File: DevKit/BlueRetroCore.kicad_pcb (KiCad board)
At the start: 4 copper layers, 85 x 56 mm, 106 parts, among them J1 USB_C_Receptacle_USB2.0, J2 Conn_02x06, J3 Micro_SD_Card, J4 Conn_01x03, J5 DB25_Female, J6 Conn_02x13, J7 Conn_02x07, Q1 BSS138, Q2 BSS138, Q3 S8050, Q4 S8050, Q5 S8050, SW1 BOOT, SW2 EN, U1 ESP32-WROOM-32E, U10 TPD6F003, U11 TPD6F003, U12 TPD6F003, U13 TPD6F003, U2 FT2232HL, U3 STL6N3LLH6, U4 TCPP01-M12, U5 M93C46, U6 ECMF02-2AMX6, U7 TPD6F003, U8 AP7361C-33E, U9 AP7361C-33E, Y1 12MHz

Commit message: PCB revision v1.1
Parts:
- U10, U11, U12, U13, U7: value TPD6F003 -> TPD6F002DSVR; footprint BlueRetro:Texas_R-PWSON-N12_EP0.4x2mm -> BlueRetro:Texas_DVS_R-PWSON-N12
- moved U10 3.29 mm to (16.5, -12.0)
- moved U12 3.12 mm to (16.5, 6.00)
- moved U11 2.66 mm to (16.5, -2.50)
- moved U13 2.65 mm to (16.5, 10.8)
- moved D10 2.49 mm to (12.9, 11.9)
- moved D9 2.38 mm to (14.1, 14.7)
- moved U7 0.79 mm to (-39.0, -8.50)
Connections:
- J2 pad 3: /IO1 -> /IO3
- J2 pad 5: /IO3 -> /IO1
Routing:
- net /IO3: track 40.9 -> 32.8 mm
- net /IO25: track 42.1 -> 38.6 mm
- net /IO21: track 12.1 -> 8.59 mm
- net /IO19: track 11.2 -> 7.74 mm
- net /IO23: track 13.7 -> 10.3 mm
- net /I34_C: track 13.2 -> 16.5 mm
- net /IO22: track 13.2 -> 9.87 mm
- net /IO19_C: track 15.3 -> 18.5 mm
- net /I35_C: track 16.6 -> 19.9 mm
- net /VIN_C: track 48.8 -> 45.6 mm
- net /IO32_C: track 14.0 -> 17.2 mm
- net /I39_C: track 16.0 -> 19.1 mm
- net /IO33: track 42.8 -> 39.9 mm
- net /IO25_C: track 15.5 -> 18.4 mm
- net /IO21_C: track 12.8 -> 15.5 mm
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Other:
- board text added: "3V3"
- board text added: "3V3_U"
- board text added: "5V"
- board text added: "BOOT"
- board text added: "CTS"
- board text added: "EN"
- board text added: "GND"
- board text added: "I34"
- board text added: "I35"
- board text added: "I36"
- board text added: "I39"
- board text added: "IO0"
- board text added: "IO1"
- board text added: "IO16"
- board text added: "IO17"
- board text added: "IO18"
- board text added: "IO19"
- board text added: "IO21"
- board text added: "IO22"
- board text added: "IO23"
- board text added: "IO25"
- board text added: "IO26"
- board text added: "IO27"
- board text added: "IO3"
- board text added: "IO32"
- board text added: "IO33"
- board text added: "IO5"
- board text added: "JTAG"
- board text added: "RTS"
- board text added: "RXD"
- board text added: "TCK"
- board text added: "TDI"
- board text added: "TDO"
- board text added: "TMS"
- board text added: "TXD"
- board text added: "UART"
- board text added: "VBUS"
- board text added: "VIN"
- board text added: "VOUT"
- board text added: "nTRST"
- board text added: "v1.1"
- board text added: "© 2020 Jacques Gagnon Licensed under CERN-OHL-P https://hackaday.io/project/170365-blueretro https://github.com/darthcloud/BlueRetro"
- board text removed: "v1.0"

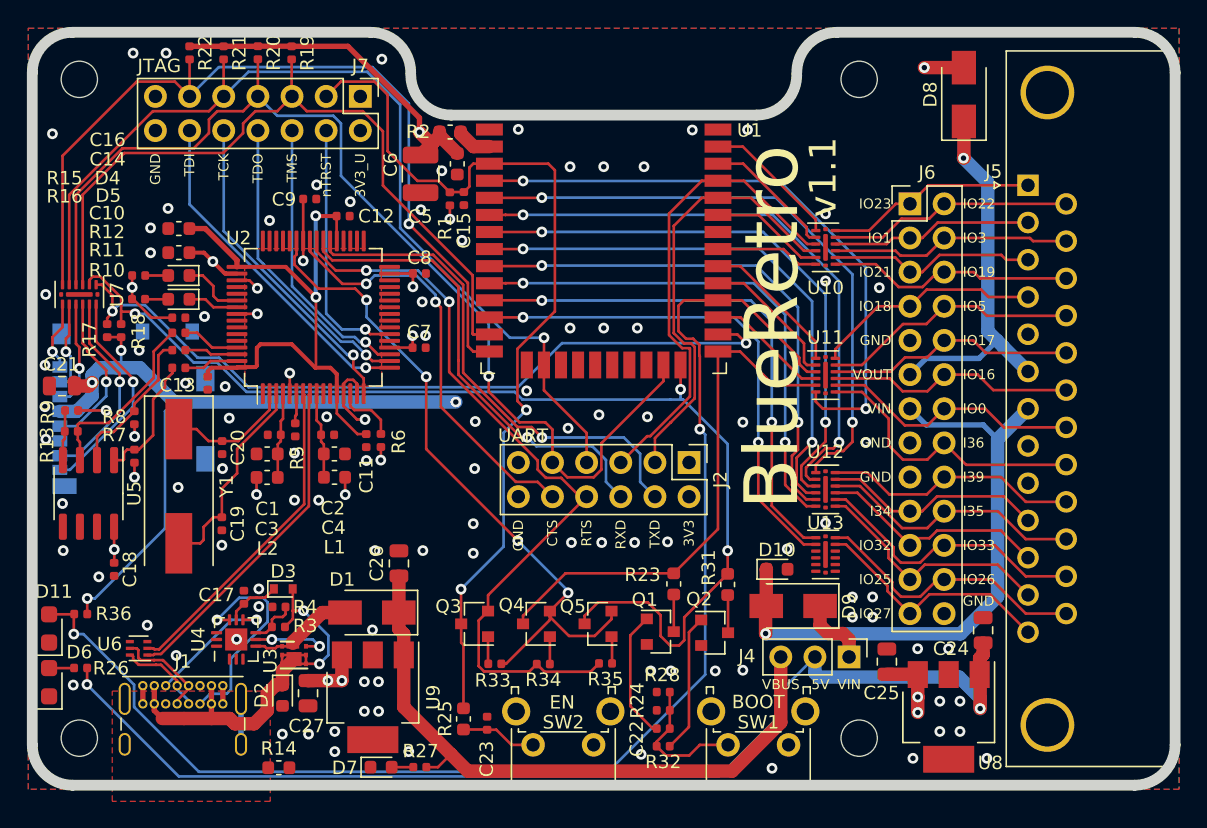
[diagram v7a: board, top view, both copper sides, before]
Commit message: Simplify BR devkit
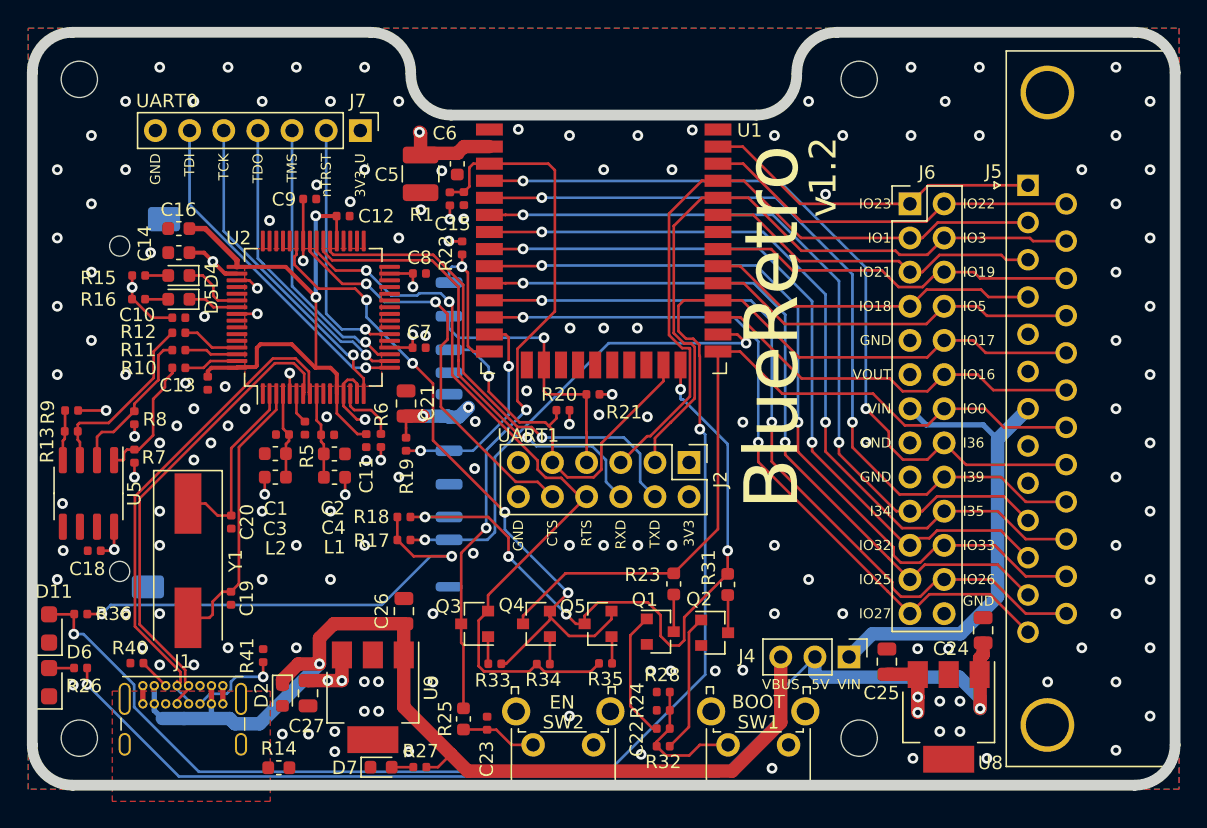
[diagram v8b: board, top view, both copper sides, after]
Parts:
- removed C17: 0.1u, BlueRetro:C_0402_1005Metric
- removed D1, D8, D9: SS14, BlueRetro:D_SMA
- removed D10: ESDA25P35-1U1M, BlueRetro:D_0603_1608Metric
- removed D3: BAT54KFILM, BlueRetro:D_SOD-523
- removed R2: 0, BlueRetro:R_0603_1608Metric
- removed R3: 10K, BlueRetro:R_0402_1005Metric
- removed R4: 2.7K, BlueRetro:R_0402_1005Metric
- removed U10, U11, U12, U13, U7: TPD6F002DSVR, BlueRetro:Texas_DVS_R-PWSON-N12
- removed U3: STL6N3LLH6, BlueRetro:POWERFLAT-2X2
- removed U4: TCPP01-M12, BlueRetro:QFN-12-1EP_3x3mm_P0.5mm_EP1.65x1.65mm
- removed U6: ECMF02-2AMX6, BlueRetro:ST_UQFN-6L_1.5x1.7mm_Pitch0.5mm
- added R40: 5.1K, BlueRetro:R_0402_1005Metric, F.Cu at (-34.7, 18.9)
- added R41: 5.1K, BlueRetro:R_0402_1005Metric, F.Cu at (-25.3, 18.4)
- J3: value Micro_SD_Card -> SD_Card; footprint BlueRetro:microSD_HC_Molex_104031-0811 -> Connector_Card:SD_Kyocera_145638009511859+
- J7: value Conn_02x07 -> Conn_01x07; footprint BlueRetro:PinHeader_2x07_P2.54mm_Vertical -> Connector_PinHeader_2.54mm:PinHeader_1x07_P2.54mm_Vertical
- moved R21 37.4 mm to (-0.80, -1.07), turned to 180 degrees
- moved R20 35.0 mm to (-3.03, 0.11), turned to 180 degrees
- moved R19 30.3 mm to (-14.7, 2.64)
- moved R17 27.0 mm to (-14.9, 9.76), turned to 0 degrees
- moved C21 25.6 mm to (-14.7, -0.39), turned to 90 degrees
- moved R18 25.2 mm to (-14.9, 8.05), turned to 0 degrees
- moved R22 24.9 mm to (-10.5, -12.0)
- moved J3 11.0 mm to (-24.0, 0.00), turned to 90 degrees
- moved C19 5.58 mm to (-27.7, 14.1)
- moved Y1 5.58 mm to (-30.9, 11.3)
- moved C20 5.58 mm to (-27.7, 8.43)
- moved C26 3.56 mm to (-14.9, 15.1)
- moved J7 2.54 mm to (-18.1, -20.7)
- moved C18 2.03 mm to (-37.9, 10.6), turned to 180 degrees
- moved R5 0.73 mm to (-22.2, 1.44)
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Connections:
- D2 pad 1: Net-(D2-Pad1) -> VBUS
- J1 pad A4: Net-(D2-Pad1) -> VBUS
- J1 pad A9: Net-(D2-Pad1) -> VBUS
- J1 pad B4: Net-(D2-Pad1) -> VBUS
- J1 pad B9: Net-(D2-Pad1) -> VBUS
- J3 pad 1: Net-(J3-Pad1) -> /IO13
- J3 pad 11: GND -> (no net)
- J3 pad 2: Net-(J3-Pad2) -> /IO15
- J3 pad 3: Net-(J3-Pad3) -> GND
- J3 pad 5: Net-(J3-Pad5) -> /IO14
- J3 pad 7: Net-(J3-Pad7) -> /IO2
- J3 pad 8: Net-(J3-Pad8) -> /IO4
- J3 pad 9: (no net) -> /IO12
- J5 pad 1: /IO23_C -> /IO23
- J5 pad 10: /I34_C -> /I34
- J5 pad 11: /IO32_C -> /IO32
- J5 pad 12: /IO25_C -> /IO25
- J5 pad 13: /IO27_C -> /IO27
- J5 pad 14: /IO22_C -> /IO22
- J5 pad 15: /IO3_C -> /IO3
- J5 pad 16: /IO19_C -> /IO19
- J5 pad 17: /IO5_C -> /IO5
- J5 pad 18: /IO17_C -> /IO17
- J5 pad 19: /IO16_C -> /IO16
- J5 pad 2: /IO1_C -> /IO1
- J5 pad 20: /IO0_C -> /IO0
- J5 pad 21: /I36_C -> /I36
- J5 pad 22: /I39_C -> /I39
- J5 pad 23: /I35_C -> /I35
- J5 pad 24: /IO33_C -> /IO33
- J5 pad 25: /IO26_C -> /IO26
- J5 pad 3: /IO21_C -> /IO21
- J5 pad 4: /IO18_C -> /IO18
- J5 pad 6: /VOUT_C -> +3V3
- J5 pad 7: /VIN_C -> VIN
- J6 pad 1: /IO23_C -> /IO23
- J6 pad 10: /I34_C -> /I34
- J6 pad 11: /IO32_C -> /IO32
- J6 pad 12: /IO25_C -> /IO25
- J6 pad 13: /IO27_C -> /IO27
- J6 pad 14: /IO22_C -> /IO22
- J6 pad 15: /IO3_C -> /IO3
- J6 pad 16: /IO19_C -> /IO19
- J6 pad 17: /IO5_C -> /IO5
- J6 pad 18: /IO17_C -> /IO17
- J6 pad 19: /IO16_C -> /IO16
- J6 pad 2: /IO1_C -> /IO1
- J6 pad 20: /IO0_C -> /IO0
- J6 pad 21: /I36_C -> /I36
- J6 pad 22: /I39_C -> /I39
- J6 pad 23: /I35_C -> /I35
- J6 pad 24: /IO33_C -> /IO33
- J6 pad 25: /IO26_C -> /IO26
- J6 pad 3: /IO21_C -> /IO21
- J6 pad 4: /IO18_C -> /IO18
- J6 pad 6: /VOUT_C -> +3V3
- J6 pad 7: /VIN_C -> VIN
- J7 pad 2: +3V3_USB -> /nTRST
- J7 pad 3: /EN -> /TMS
- J7 pad 4: /nTRST -> /TDO
- J7 pad 5: /IO14 -> /TCK
- J7 pad 6: /TMS -> /TDI
- J7 pad 7: /IO15 -> GND
- U1 pad 2: Net-(R2-Pad1) -> +3V3
- U2 pad 7: /USB_N -> /USB_C_N
- U2 pad 8: /USB_P -> /USB_C_P
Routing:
- net /IO12: track 64.5 -> 10.8 mm
- net /IO13: track 72.7 -> 20.6 mm
- net /IO15: track 80.5 -> 29.1 mm
- net /VIN_C: track 45.6 -> 0.00 mm, vias 1 -> 0
- net /IO14: track 55.4 -> 16.0 mm, vias 0 -> 2
- net Net-(D2-Pad1): track 35.7 -> 0.00 mm, vias 2 -> 0
- net +3V3: track 91.4 -> 58.0 mm, vias 9 -> 11
- net /IO2: track 84.0 -> 53.0 mm, vias 3 -> 5
- net /USB_C_P: track 6.49 -> 37.0 mm
- net VIN: track 5.32 -> 35.3 mm
- net /VOUT_C: track 28.1 -> 0.00 mm, vias 1 -> 0
- net /USB_C_N: track 7.56 -> 35.5 mm
- net VBUS: track 48.5 -> 75.9 mm, vias 0 -> 1
- net /USB_P: track 25.0 -> 0.00 mm
- net /USB_N: track 24.4 -> 0.00 mm
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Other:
- rule pad_to_mask_clearance: 0.05 -> 0
- board text added: "UART0"
- board text added: "UART1"
- board text added: "v1.2"
- board text added: "© 2020-2023 Jacques Gagnon Licensed under CERN-OHL-P https://github.com/darthcloud/BlueRetro"
- board text removed: "JTAG"
- board text removed: "UART"
- board text removed: "v1.1"
- board text removed: "© 2020 Jacques Gagnon Licensed under CERN-OHL-P https://hackaday.io/project/170365-blueretro https://github.com/darthcloud/BlueRetro"
